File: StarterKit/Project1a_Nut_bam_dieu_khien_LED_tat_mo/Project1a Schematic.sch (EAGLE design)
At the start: 6 parts, among them U1 ARDUINOR3-BPLACE

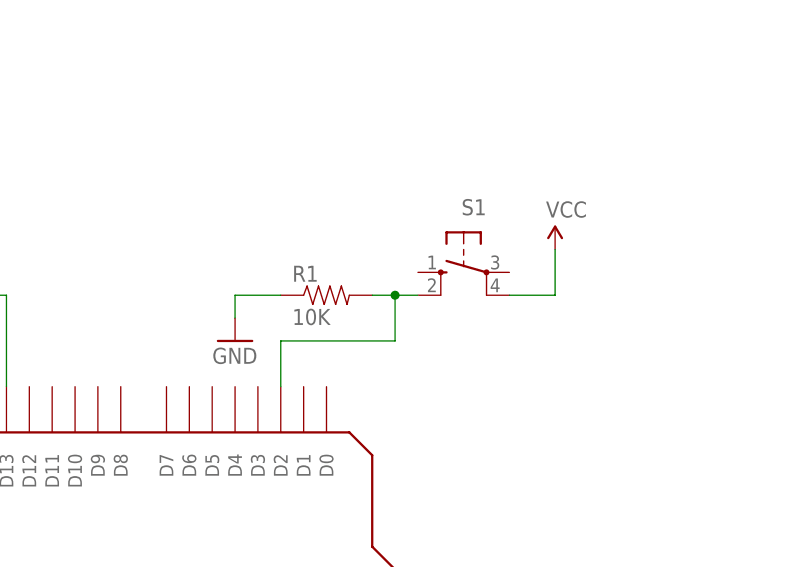
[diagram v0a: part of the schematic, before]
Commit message: Chuyen tu dien tro keo thap (pull-down) sang keo cao (pull-up) cho project 1a,1b,1c,7,11.
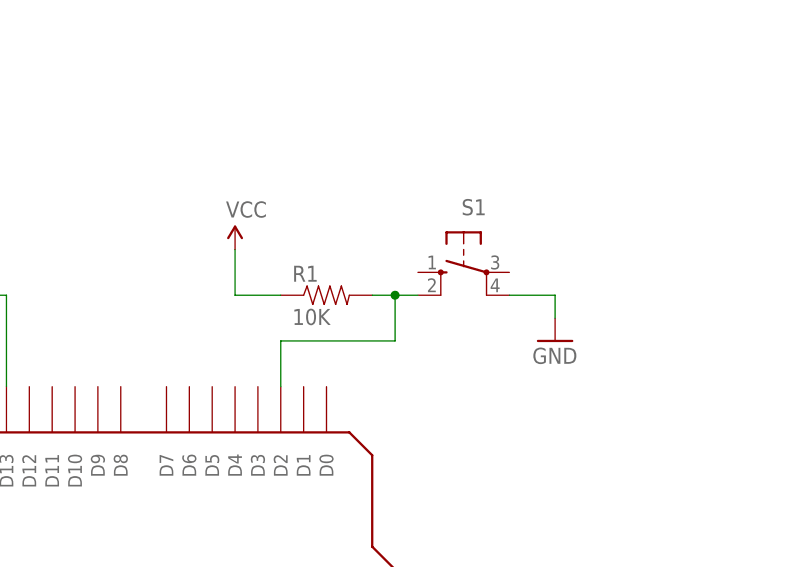
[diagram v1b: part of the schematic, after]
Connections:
- net GND: now also S1.P1; no longer R1.1
- net VCC: now also R1.1; no longer S1.P1
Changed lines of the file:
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@@
 <setting verticaltext="up"/>
 </settings>
-<grid distance="0.1" unitdist="inch" unit="inch" style="dots" multiple="1" display="yes" altdistance="0.01" altunitdist="inch" altunit="inch"/>
+<grid distance="0.1" unitdist="inch" unit="inch" style="lines" multiple="1" display="no" altdistance="0.01" altunitdist="inch" altunit="inch"/>
 <layers>
 <layer number="1" name="Top" color="4" fill="1" visible="no" active="no"/>
@@
 <instance part="LED1" gate="G$1" x="38.1" y="119.38" rot="R270"/>
 <instance part="GND2" gate="1" x="27.94" y="109.22"/>
-<instance part="GND3" gate="1" x="88.9" y="114.3"/>
-<instance part="SUPPLY2" gate="G$1" x="124.46" y="124.46"/>
+<instance part="GND3" gate="1" x="124.46" y="114.3"/>
+<instance part="SUPPLY2" gate="G$1" x="88.9" y="124.46"/>
 <instance part="FRAME1" gate="G$1" x="-33.02" y="-15.24"/>
 <instance part="FRAME1" gate="V" x="114.3" y="-15.24"/>
@@
 </segment>
 <segment>
-<pinref part="S1" gate="1" pin="P1"/>
 <pinref part="SUPPLY2" gate="G$1" pin="VCC"/>
-<wire x1="119.38" y1="119.38" x2="124.46" y2="119.38" width="0.1524" layer="91"/>
-<wire x1="124.46" y1="119.38" x2="124.46" y2="124.46" width="0.1524" layer="91"/>
+<wire x1="88.9" y1="124.46" x2="88.9" y2="119.38" width="0.1524" layer="91"/>
+<pinref part="R1" gate="G$1" pin="1"/>
+<wire x1="88.9" y1="119.38" x2="93.98" y2="119.38" width="0.1524" layer="91"/>
 </segment>
 </net>
@@
 </segment>
 <segment>
+<pinref part="S1" gate="1" pin="P1"/>
 <pinref part="GND3" gate="1" pin="GND"/>
-<wire x1="88.9" y1="116.84" x2="88.9" y2="119.38" width="0.1524" layer="91"/>
-<pinref part="R1" gate="G$1" pin="1"/>
-<wire x1="88.9" y1="119.38" x2="93.98" y2="119.38" width="0.1524" layer="91"/>
+<wire x1="119.38" y1="119.38" x2="124.46" y2="119.38" width="0.1524" layer="91"/>
+<wire x1="124.46" y1="119.38" x2="124.46" y2="116.84" width="0.1524" layer="91"/>
 </segment>
 </net>
